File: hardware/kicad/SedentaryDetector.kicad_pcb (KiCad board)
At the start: 2 copper layers, 6 parts, among them J1 ESP32_2x15, J2 MPU6050_1x8

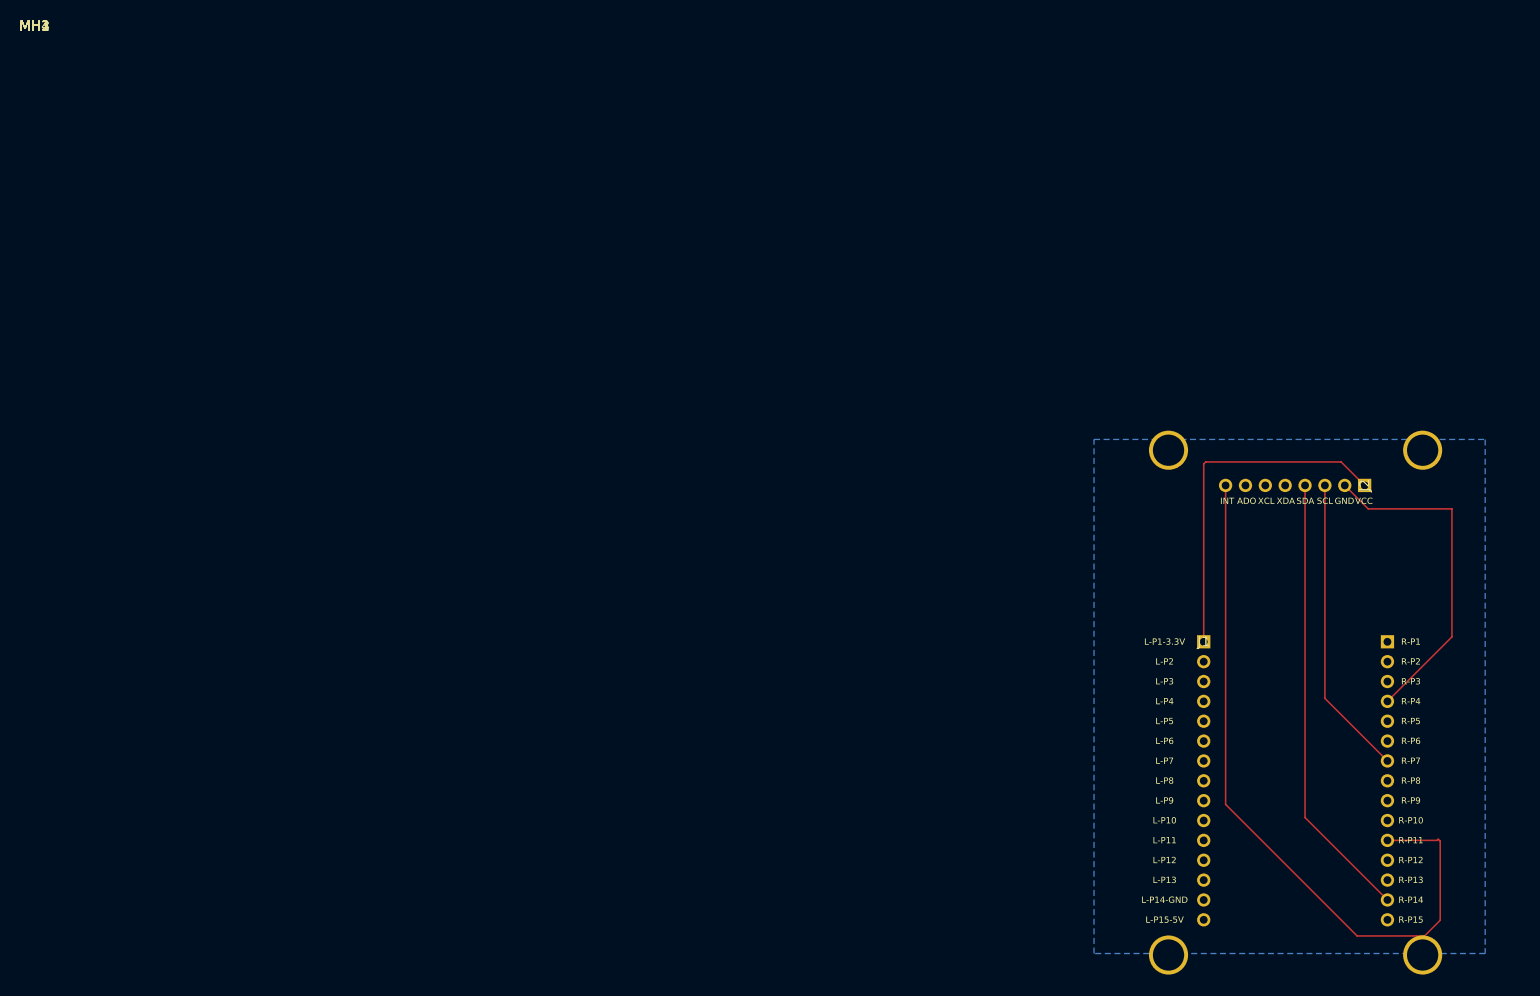
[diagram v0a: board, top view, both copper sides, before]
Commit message: feat(hardware): add board outline through MH
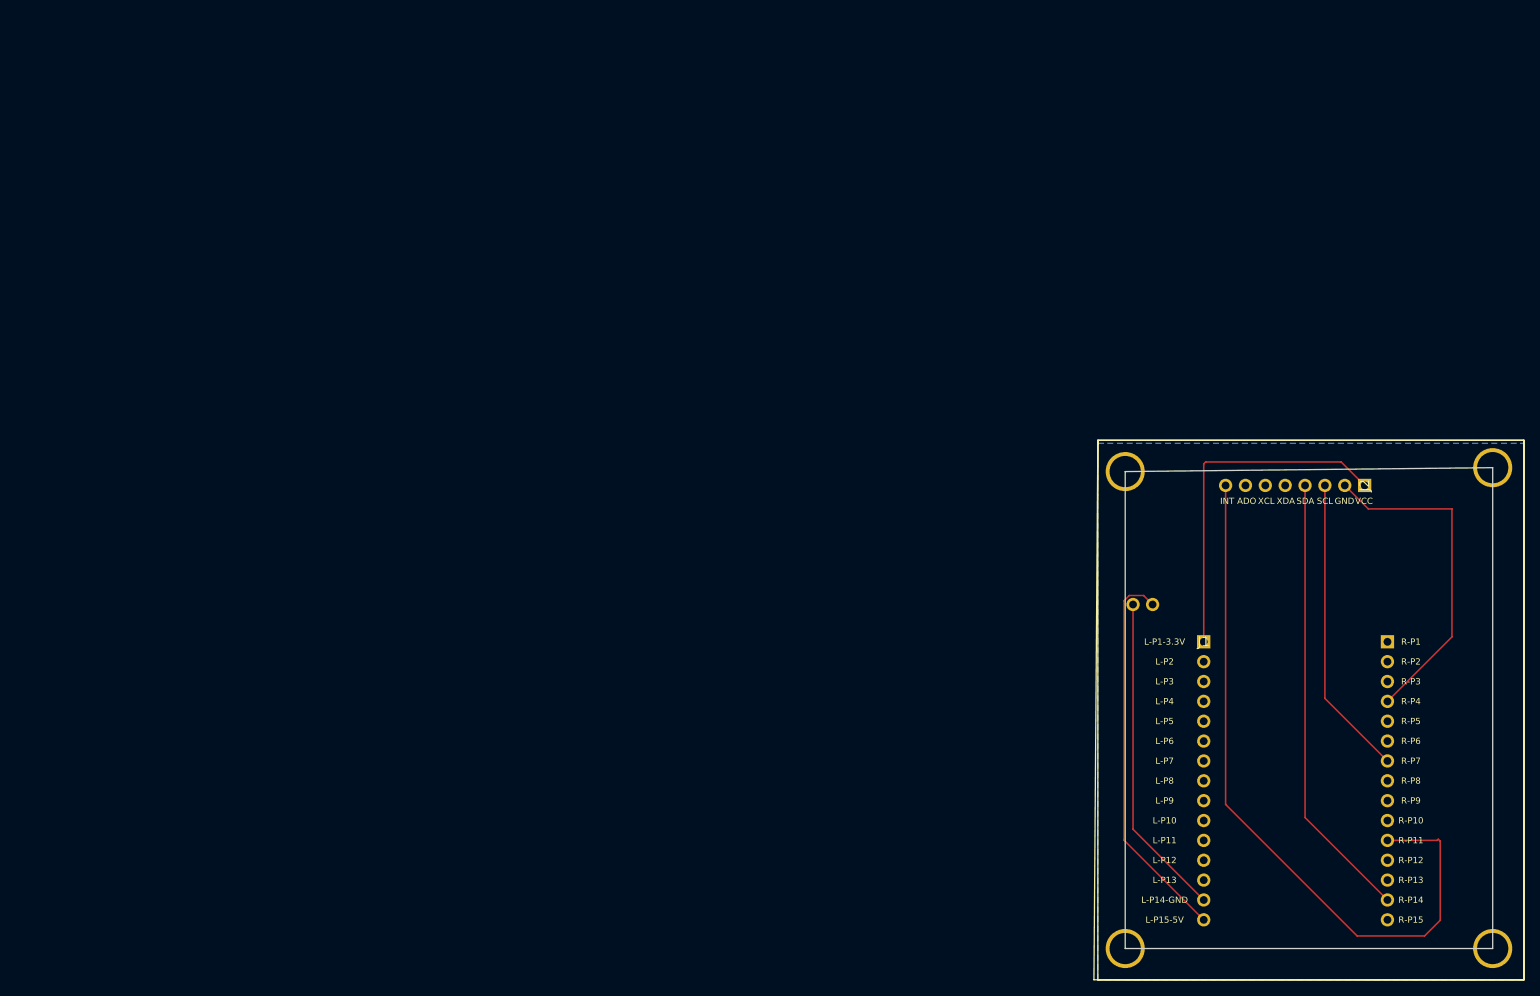
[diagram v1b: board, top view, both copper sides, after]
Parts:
- added ?: , , F.Cu at (143.0, 74.0)
- added ?: , , F.Cu at (140.5, 74.0)
- moved MH2 9.23 mm to (8.96, 2.23)
- moved MH3 9.00 mm to (8.96, -0.83)
- moved MH1 6.18 mm to (-5.54, 2.73)
- moved MH4 5.60 mm to (-5.54, -0.83)
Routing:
- net unconnected-(J1-Pad15): track 0.00 -> 49.4 mm
- net GND: track 43.0 -> 84.5 mm
- added copper zone on B.Cu, net (none)
- removed copper zone on B.Cu, net GND
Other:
- board outline added: 47 x 61.5 mm

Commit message: fix(hardware): border 3mm outside MH, 53x68mm
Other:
- board size 47 x 61.5 mm -> 53 x 67.5 mm
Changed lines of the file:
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@@
 	)
 	(gr_line
-		(start 139.5 57)
-		(end 186.5 56.5)
+		(start 136.5 53.5)
+		(end 189.5 53.5)
 		(stroke
 			(width 0.1)
@@
 	)
 	(gr_line
-		(start 139.5 118)
-		(end 139.5 57)
+		(start 136.5 121)
+		(end 136.5 53.5)
 		(stroke
 			(width 0.1)
@@
 	)
 	(gr_line
-		(start 186.5 56.5)
-		(end 186.5 118)
+		(start 189.5 53.5)
+		(end 189.5 121)
 		(stroke
 			(width 0.1)
@@
 	)
 	(gr_line
-		(start 186.5 118)
-		(end 139.5 118)
+		(start 189.5 121)
+		(end 136.5 121)
 		(stroke
 			(width 0.1)

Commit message: V0.4: Gerber export ready, J3 power, M4 holes
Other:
- board size 53 x 67.5 mm -> 54.5 x 69 mm
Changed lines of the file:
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@@
-		(layer "F.SilkS")
-	)
-	(gr_rect
-		(start 136 53)
-		(end 190.5 122)
-		(stroke
-			(width 0.1)
-			(type default)
-		)
-		(fill no)
 		(layer "F.SilkS")
 	)
@@
 		(layer "F.SilkS")
 	)
-	(gr_line
-		(start 136.5 53.5)
-		(end 189.5 53.5)
+	(gr_rect
+		(start 136 53)
+		(end 190.5 122)
 		(stroke
 			(width 0.1)
 			(type default)
 		)
+		(fill no)
 		(layer "Edge.Cuts")
 	)
-	(gr_line
-		(start 136.5 121)
-		(end 136.5 53.5)
-		(stroke
-			(width 0.1)
-			(type default)
-		)
-		(layer "Edge.Cuts")
-	)
-	(gr_line
-		(start 189.5 53.5)
-		(end 189.5 121)
-		(stroke
-			(width 0.1)
-			(type default)
-		)
-		(layer "Edge.Cuts")
-	)
-	(gr_line
-		(start 189.5 121)
-		(end 136.5 121)
-		(stroke
-			(width 0.1)
-			(type default)
-		)
-		(layer "Edge.Cuts")
-	)

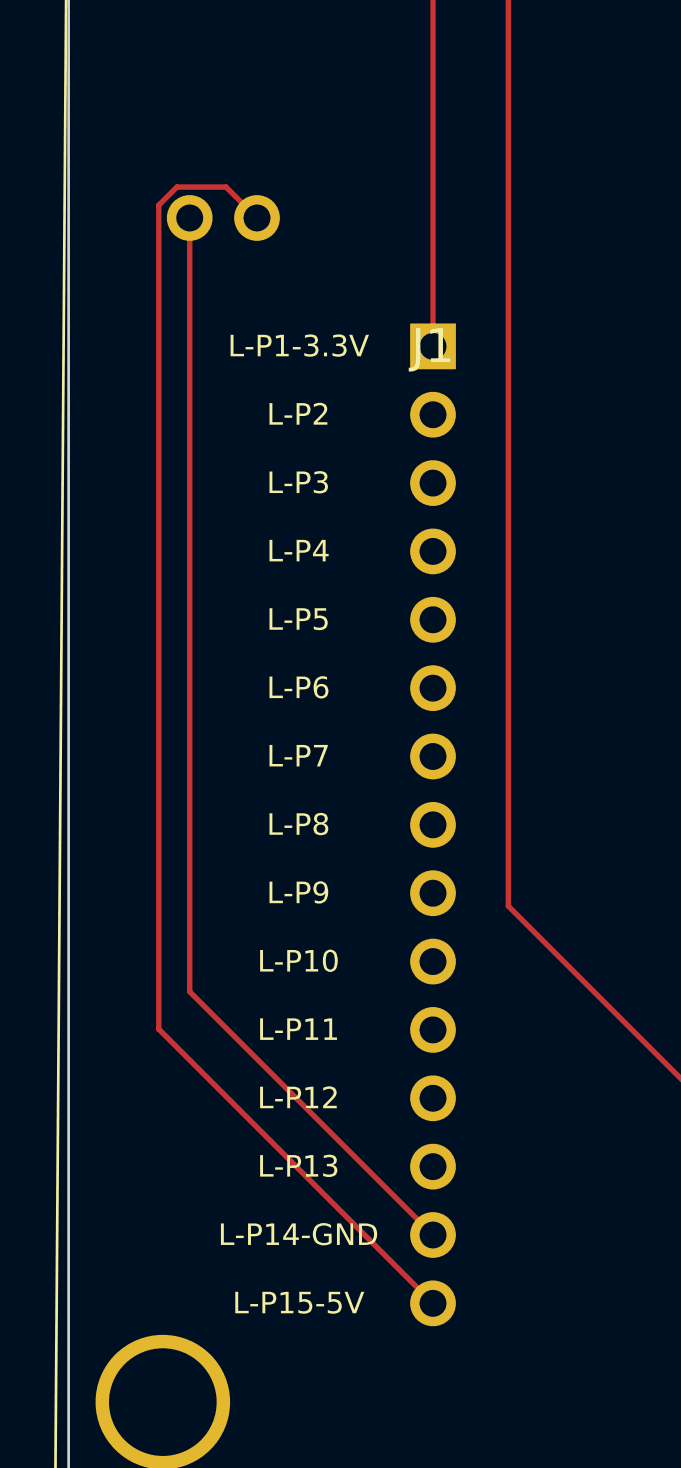
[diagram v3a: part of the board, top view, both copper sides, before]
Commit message: chore(hardware): clean up directory structure
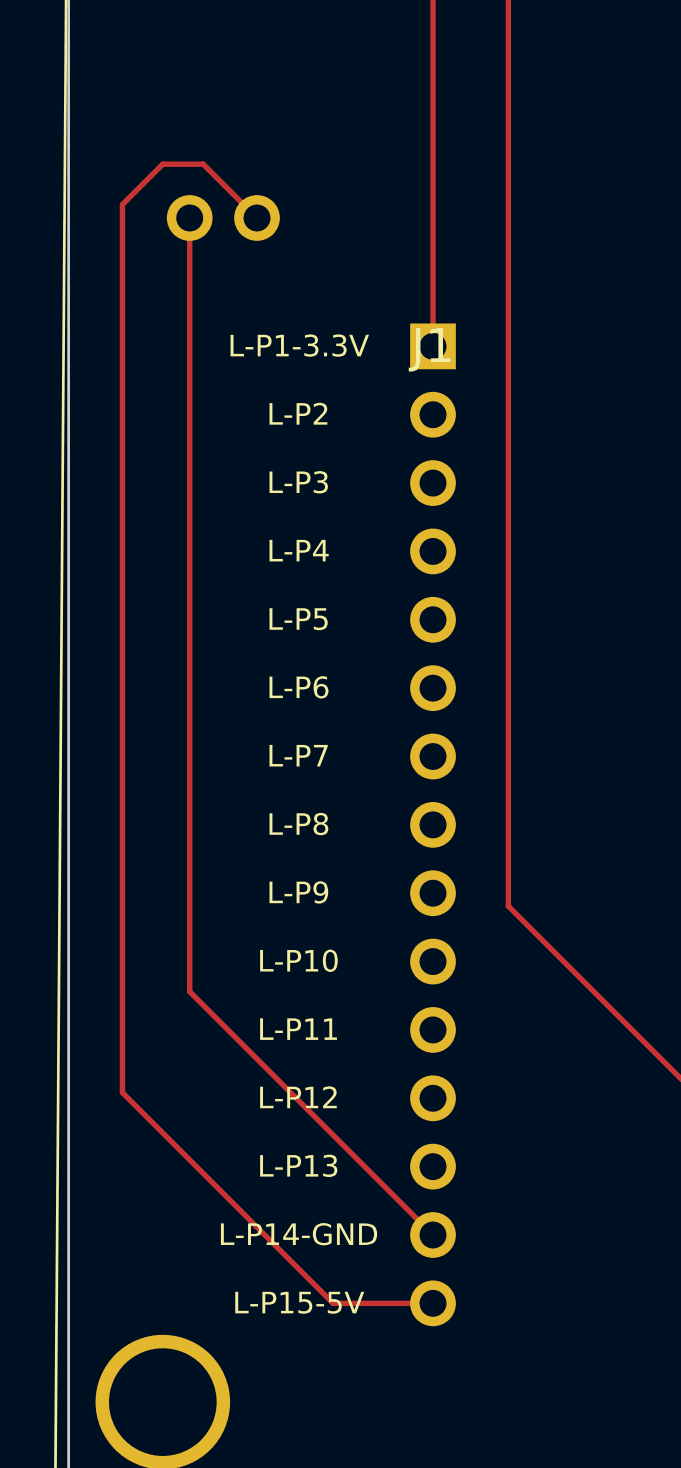
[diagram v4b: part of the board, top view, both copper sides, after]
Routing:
- net unconnected-(J1-Pad15): track 49.4 -> 54.2 mm
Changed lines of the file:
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@@
 	)
 	(segment
-		(start 139.35 104.14)
+		(start 138 73.5)
+		(end 138 106.5)
+		(width 0.2)
+		(layer "F.Cu")
+		(net "unconnected-(J1-Pad15)")
+	)
+	(segment
+		(start 139.5 72)
+		(end 138 73.5)
+		(width 0.2)
+		(layer "F.Cu")
+		(net "unconnected-(J1-Pad15)")
+	)
+	(segment
+		(start 141 72)
+		(end 139.5 72)
+		(width 0.2)
+		(layer "F.Cu")
+		(net "unconnected-(J1-Pad15)")
+	)
+	(segment
+		(start 138 106.5)
+		(end 145.83 114.33)
+		(width 0.2)
+		(layer "F.Cu")
+		(net "unconnected-(J1-Pad15)")
+	)
+	(segment
+		(start 145.83 114.33)
 		(end 149.54 114.33)
 		(width 0.2)
@@
 	)
 	(segment
-		(start 141.85 72.85)
-		(end 140.023654 72.85)
+		(start 143 74)
+		(end 141 72)
 		(width 0.2)
 		(layer "F.Cu")
-		(net "unconnected-(J1-Pad15)")
-	)
-	(segment
-		(start 140.023654 72.85)
-		(end 139.35 73.523654)
-		(width 0.2)
-		(layer "F.Cu")
-		(net "unconnected-(J1-Pad15)")
-	)
-	(segment
-		(start 139.35 73.523654)
-		(end 139.35 104.14)
-		(width 0.2)
-		(layer "F.Cu")
-		(net "unconnected-(J1-Pad15)")
-	)
-	(segment
-		(start 143 74)
-		(end 141.85 72.85)
-		(width 0.2)
-		(layer "F.Cu")
